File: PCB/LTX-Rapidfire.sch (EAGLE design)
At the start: 47 parts, among them J1 F-1X08-SIP-100-40Y, Q1 2N3904, Q10 SS8550D, Q11 2N3906, Q13 2N3904, Q2 2N3906, Q3 2N3904, Q4 2N3904, Q5 2N3904, Q6 2N3906, Q7 2N3906, Q8 2N3906, Q9 2N3904, SW1 F-1X02-SIP-100-40

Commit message: Whoops. Missed some bits. /Now/ it's complete.
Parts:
- added Q12: 2N3906, transistor-pnp:2N3906
- added R22: 100k, rcl:R-US_0204/2V
- added R23: 1k, rcl:R-US_0204/7
- added R26: 10k, rcl:R-US_0204/7
- R21: value 10k -> 200k
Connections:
- new net N$17: Q12.C, R23.1
- new net N$20: Q12.B, R21.2, R22.2
- net PA2: now also R26.2; no longer R21.2
- net PGND: now also R22.1
- net SGND: now also R23.2
- net SW9V: now also R21.1
- net VCC: now also Q12.E, R26.1; no longer R21.1
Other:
- moved on the sheet: R21
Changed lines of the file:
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@@
 <part name="U$1" library="izzy" deviceset="Z8F082A" device="DIL-8"/>
 <part name="SV1" library="izzy" deviceset="MA03-2" device=""/>
-<part name="R21" library="rcl" deviceset="R-US_" device="0204/7" value="10k"/>
+<part name="R26" library="rcl" deviceset="R-US_" device="0204/7" value="10k"/>
+<part name="R21" library="rcl" deviceset="R-US_" device="0204/7" value="200k"/>
+<part name="R22" library="rcl" deviceset="R-US_" device="0204/2V" value="100k"/>
+<part name="R23" library="rcl" deviceset="R-US_" device="0204/7" value="1k"/>
+<part name="Q12" library="transistor-pnp" deviceset="2N3906" device=""/>
 </parts>
 <sheets>
@@
 <instance part="U$1" gate="G$1" x="175.26" y="81.28"/>
 <instance part="SV1" gate="1" x="142.24" y="45.72"/>
-<instance part="R21" gate="G$1" x="142.24" y="35.56" rot="R180"/>
+<instance part="R26" gate="G$1" x="142.24" y="35.56" rot="R180"/>
+<instance part="R21" gate="G$1" x="88.9" y="50.8" rot="R270"/>
+<instance part="R22" gate="G$1" x="88.9" y="35.56" rot="R90"/>
+<instance part="R23" gate="G$1" x="106.68" y="30.48" rot="R270"/>
+<instance part="Q12" gate="G$1" x="104.14" y="43.18"/>
 </instances>
 <busses>
@@
 <label x="238.76" y="198.12" size="1.778" layer="95"/>
 </segment>
+<segment>
+<pinref part="R21" gate="G$1" pin="1"/>
+<wire x1="88.9" y1="55.88" x2="88.9" y2="58.42" width="0.1524" layer="91"/>
+<label x="88.9" y="58.42" size="1.778" layer="95" rot="R90"/>
+</segment>
 </net>
 <net name="LAZERMOD" class="0">
@@
 <label x="154.94" y="48.26" size="1.778" layer="95"/>
 </segment>
+<segment>
+<pinref part="R23" gate="G$1" pin="2"/>
+<wire x1="106.68" y1="25.4" x2="106.68" y2="22.86" width="0.1524" layer="91"/>
+<label x="106.68" y="22.86" size="1.778" layer="95" rot="R270"/>
+</segment>
 </net>
 <net name="PGND" class="0">
@@
 <wire x1="215.9" y1="177.8" x2="215.9" y2="175.26" width="0.1524" layer="91"/>
 <label x="215.9" y="175.26" size="1.778" layer="95" rot="R270"/>
+</segment>
+<segment>
+<pinref part="R22" gate="G$1" pin="1"/>
+<wire x1="88.9" y1="30.48" x2="88.9" y2="27.94" width="0.1524" layer="91"/>
+<label x="88.9" y="27.94" size="1.778" layer="95" rot="R270"/>
 </segment>
 </net>
@@
 <junction x="152.4" y="43.18"/>
 <label x="154.94" y="43.18" size="1.778" layer="95"/>
-<pinref part="R21" gate="G$1" pin="1"/>
+<pinref part="R26" gate="G$1" pin="1"/>
+</segment>
+<segment>
+<pinref part="Q12" gate="G$1" pin="E"/>
+<wire x1="106.68" y1="48.26" x2="106.68" y2="58.42" width="0.1524" layer="91"/>
+<label x="106.68" y="58.42" size="1.778" layer="95" rot="R90"/>
 </segment>
 </net>
@@
 <junction x="132.08" y="43.18"/>
 <label x="129.54" y="43.18" size="1.778" layer="95" rot="R180"/>
-<pinref part="R21" gate="G$1" pin="2"/>
+<pinref part="R26" gate="G$1" pin="2"/>
 </segment>
 </net>
@@
 </segment>
 </net>
+<net name="N$17" class="0">
+<segment>
+<pinref part="Q12" gate="G$1" pin="C"/>
+<pinref part="R23" gate="G$1" pin="1"/>
+<wire x1="106.68" y1="35.56" x2="106.68" y2="38.1" width="0.1524" layer="91"/>
+</segment>
+</net>
+<net name="N$20" class="0">
+<segment>
+<pinref part="R21" gate="G$1" pin="2"/>
+<pinref part="R22" gate="G$1" pin="2"/>
+<wire x1="88.9" y1="45.72" x2="88.9" y2="43.18" width="0.1524" layer="91"/>
+<pinref part="Q12" gate="G$1" pin="B"/>
+<wire x1="88.9" y1="43.18" x2="88.9" y2="40.64" width="0.1524" layer="91"/>
+<wire x1="101.6" y1="43.18" x2="88.9" y2="43.18" width="0.1524" layer="91"/>
+<junction x="88.9" y="43.18"/>
+</segment>
+</net>

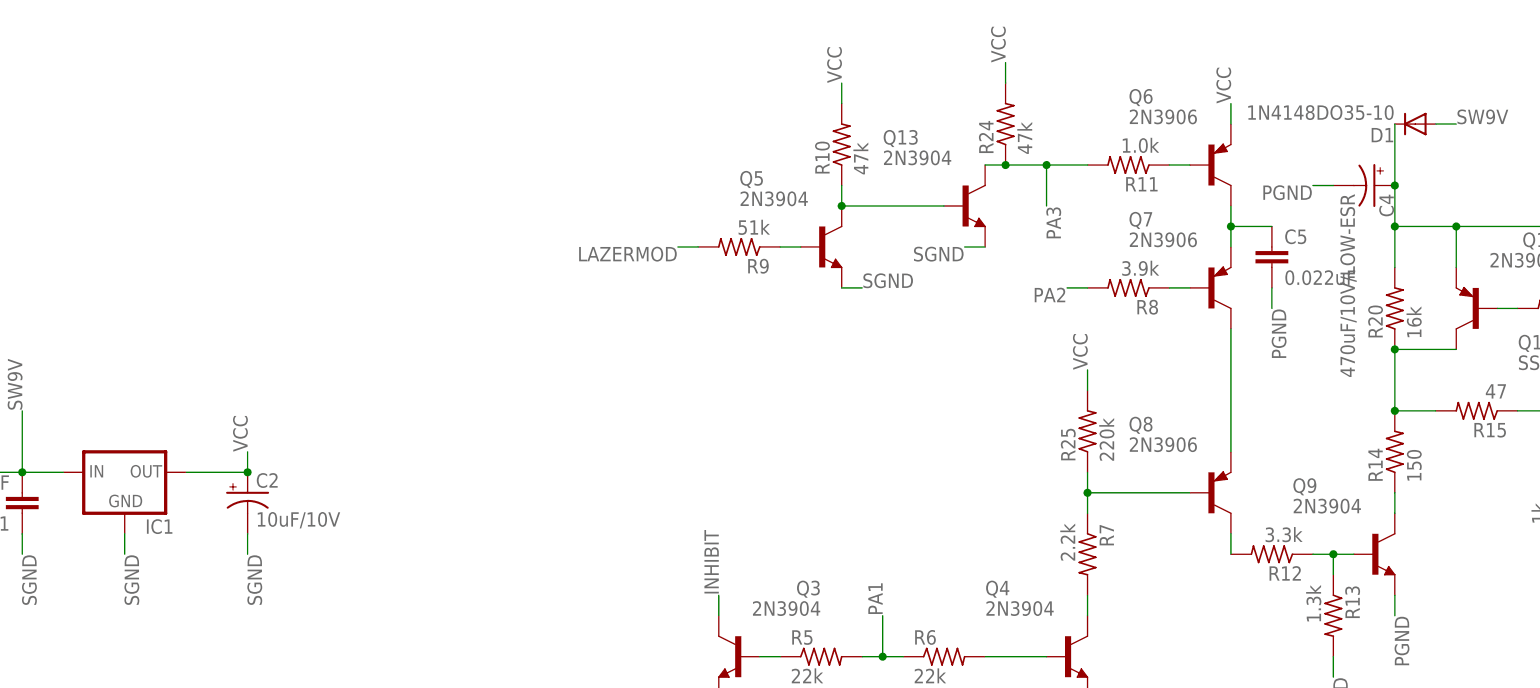
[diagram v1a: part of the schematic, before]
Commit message: First pass of PCB layout is complete.
Cleanup is in progress, but they should technically work as-is. Labels
are going to be impossible to see, though.
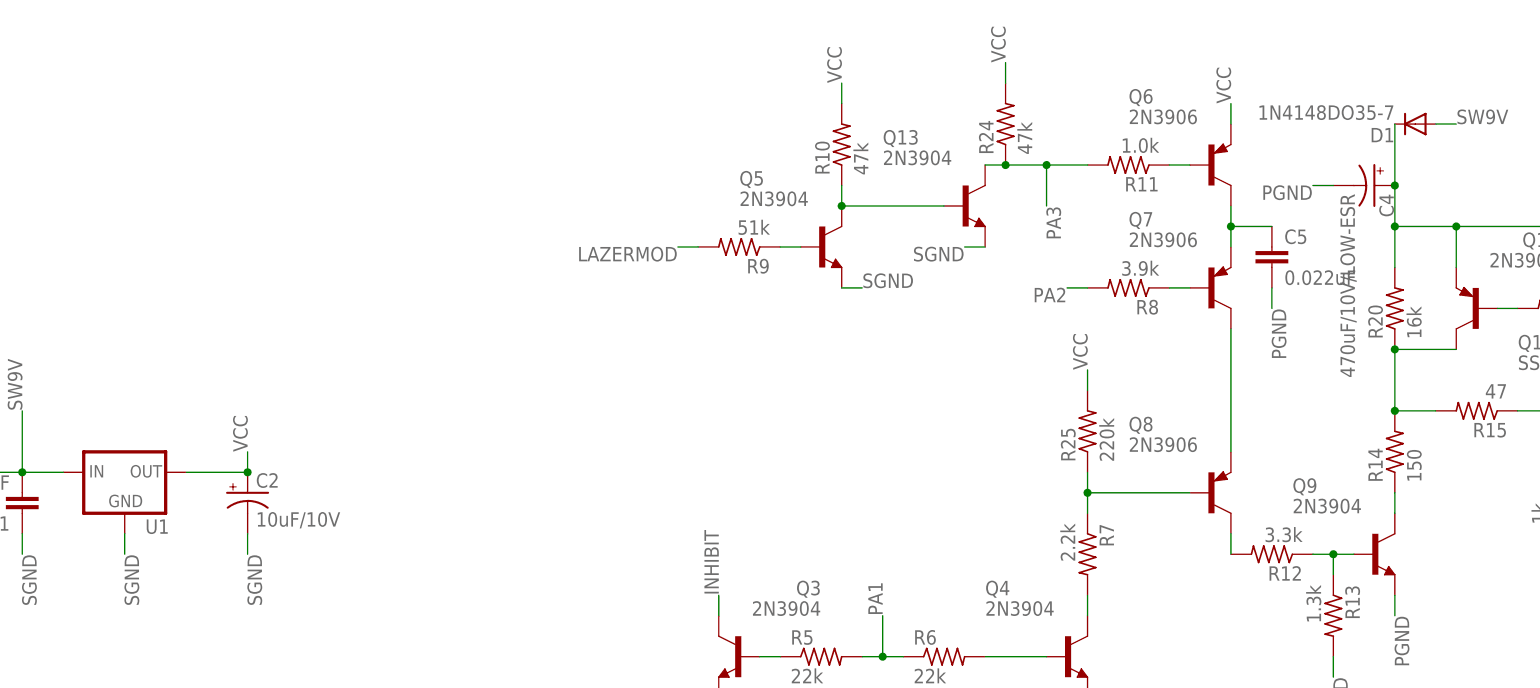
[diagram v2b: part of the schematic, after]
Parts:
- D1: value 1N4148DO35-10 -> 1N4148DO35-7; device diode:1N4148DO35-10 -> diode:1N4148DO35-7
- R26: device rcl:R-US_0204/7 -> rcl:R-US_0204/2V
- renumbered IC1 to U1
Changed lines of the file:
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@@
 <grid distance="0.1" unitdist="inch" unit="inch" style="lines" multiple="1" display="no" altdistance="0.01" altunitdist="inch" altunit="inch"/>
 <layers>
-<layer number="1" name="Top" color="4" fill="1" visible="no" active="no"/>
-<layer number="16" name="Bottom" color="1" fill="1" visible="no" active="no"/>
-<layer number="17" name="Pads" color="2" fill="1" visible="no" active="no"/>
-<layer number="18" name="Vias" color="2" fill="1" visible="no" active="no"/>
-<layer number="19" name="Unrouted" color="6" fill="1" visible="no" active="no"/>
-<layer number="20" name="Dimension" color="15" fill="1" visible="no" active="no"/>
-<layer number="21" name="tPlace" color="7" fill="1" visible="no" active="no"/>
-<layer number="22" name="bPlace" color="7" fill="1" visible="no" active="no"/>
-<layer number="23" name="tOrigins" color="15" fill="1" visible="no" active="no"/>
-<layer number="24" name="bOrigins" color="15" fill="1" visible="no" active="no"/>
-<layer number="25" name="tNames" color="7" fill="1" visible="no" active="no"/>
-<layer number="26" name="bNames" color="7" fill="1" visible="no" active="no"/>
-<layer number="27" name="tValues" color="7" fill="1" visible="no" active="no"/>
-<layer number="28" name="bValues" color="7" fill="1" visible="no" active="no"/>
+<layer number="1" name="Top" color="4" fill="1" visible="yes" active="no"/>
+<layer number="16" name="Bottom" color="1" fill="1" visible="yes" active="no"/>
+<layer number="17" name="Pads" color="2" fill="1" visible="yes" active="no"/>
+<layer number="18" name="Vias" color="2" fill="1" visible="yes" active="no"/>
+<layer number="19" name="Unrouted" color="6" fill="1" visible="yes" active="no"/>
+<layer number="20" name="Dimension" color="15" fill="1" visible="yes" active="no"/>
+<layer number="21" name="tPlace" color="7" fill="1" visible="yes" active="no"/>
+<layer number="22" name="bPlace" color="7" fill="1" visible="yes" active="no"/>
+<layer number="23" name="tOrigins" color="15" fill="1" visible="yes" active="no"/>
+<layer number="24" name="bOrigins" color="15" fill="1" visible="yes" active="no"/>
+<layer number="25" name="tNames" color="7" fill="1" visible="yes" active="no"/>
+<layer number="26" name="bNames" color="7" fill="1" visible="yes" active="no"/>
+<layer number="27" name="tValues" color="7" fill="1" visible="yes" active="no"/>
+<layer number="28" name="bValues" color="7" fill="1" visible="yes" active="no"/>
 <layer number="29" name="tStop" color="7" fill="3" visible="no" active="no"/>
 <layer number="30" name="bStop" color="7" fill="6" visible="no" active="no"/>
@@
 <layer number="35" name="tGlue" color="7" fill="4" visible="no" active="no"/>
 <layer number="36" name="bGlue" color="7" fill="5" visible="no" active="no"/>
-<layer number="37" name="tTest" color="7" fill="1" visible="no" active="no"/>
-<layer number="38" name="bTest" color="7" fill="1" visible="no" active="no"/>
+<layer number="37" name="tTest" color="7" fill="1" visible="yes" active="no"/>
+<layer number="38" name="bTest" color="7" fill="1" visible="yes" active="no"/>
 <layer number="39" name="tKeepout" color="4" fill="11" visible="no" active="no"/>
 <layer number="40" name="bKeepout" color="1" fill="11" visible="no" active="no"/>
@@
 <layer number="44" name="Drills" color="7" fill="1" visible="no" active="no"/>
 <layer number="45" name="Holes" color="7" fill="1" visible="no" active="no"/>
-<layer number="46" name="Milling" color="3" fill="1" visible="no" active="no"/>
-<layer number="47" name="Measures" color="7" fill="1" visible="no" active="no"/>
-<layer number="48" name="Document" color="7" fill="1" visible="no" active="no"/>
-<layer number="49" name="Reference" color="7" fill="1" visible="no" active="no"/>
-<layer number="50" name="dxf" color="7" fill="1" visible="no" active="no"/>
-<layer number="51" name="tDocu" color="7" fill="1" visible="no" active="no"/>
-<layer number="52" name="bDocu" color="7" fill="1" visible="no" active="no"/>
-<layer number="53" name="tGND_GNDA" color="7" fill="9" visible="no" active="no"/>
-<layer number="54" name="bGND_GNDA" color="1" fill="9" visible="no" active="no"/>
-<layer number="56" name="wert" color="7" fill="1" visible="no" active="no"/>
+<layer number="46" name="Milling" color="3" fill="1" visible="yes" active="no"/>
+<layer number="47" name="Measures" color="7" fill="1" visible="yes" active="no"/>
+<layer number="48" name="Document" color="7" fill="1" visible="yes" active="no"/>
+<layer number="49" name="Reference" color="7" fill="1" visible="yes" active="no"/>
+<layer number="50" name="dxf" color="7" fill="1" visible="yes" active="no"/>
+<layer number="51" name="tDocu" color="7" fill="1" visible="yes" active="no"/>
+<layer number="52" name="bDocu" color="7" fill="1" visible="yes" active="no"/>
+<layer number="53" name="tGND_GNDA" color="7" fill="9" visible="yes" active="no"/>
+<layer number="54" name="bGND_GNDA" color="1" fill="9" visible="yes" active="no"/>
+<layer number="56" name="wert" color="7" fill="1" visible="yes" active="no"/>
 <layer number="91" name="Nets" color="2" fill="1" visible="yes" active="yes"/>
 <layer number="92" name="Busses" color="1" fill="1" visible="yes" active="yes"/>
@@
 <part name="FRAME1" library="frames" deviceset="FRAME_A_L" device=""/>
 <part name="J1" library="con-headers-jp" deviceset="F-1X08-" device="SIP-100-40Y"/>
-<part name="IC1" library="v-reg" deviceset="78LXX" device=""/>
+<part name="U1" library="v-reg" deviceset="78LXX" device=""/>
 <part name="C1" library="rcl" deviceset="C-EU" device="025-025X050" value="0.1uF"/>
 <part name="C2" library="rcl" deviceset="CPOL-US" device="E2-4" value="10uF/10V"/>
-<part name="D1" library="diode" deviceset="1N4148" device="DO35-10"/>
+<part name="D1" library="diode" deviceset="1N4148" device="DO35-7" value="1N4148DO35-7"/>
 <part name="C4" library="rcl" deviceset="CPOL-US" device="E3.5-8" value="470uF/10V/LOW-ESR"/>
 <part name="R20" library="rcl" deviceset="R-US_" device="0204/2V" value="16k"/>
@@
 <part name="U$1" library="izzy" deviceset="Z8F082A" device="DIL-8"/>
 <part name="SV1" library="izzy" deviceset="MA03-2" device=""/>
-<part name="R26" library="rcl" deviceset="R-US_" device="0204/7" value="10k"/>
+<part name="R26" library="rcl" deviceset="R-US_" device="0204/2V" value="10k"/>
 <part name="R21" library="rcl" deviceset="R-US_" device="0204/7" value="200k"/>
 <part name="R22" library="rcl" deviceset="R-US_" device="0204/2V" value="100k"/>
@@
 <instance part="FRAME1" gate="G$2" x="172.72" y="0"/>
 <instance part="J1" gate="G$1" x="25.4" y="147.32" rot="MR0"/>
-<instance part="IC1" gate="1" x="73.66" y="154.94"/>
+<instance part="U1" gate="1" x="73.66" y="154.94"/>
 <instance part="C1" gate="G$1" x="60.96" y="149.86" rot="R180"/>
 <instance part="C2" gate="G$1" x="88.9" y="152.4"/>
@@
 <segment>
 <pinref part="C1" gate="G$1" pin="2"/>
-<pinref part="IC1" gate="1" pin="IN"/>
+<pinref part="U1" gate="1" pin="IN"/>
 <wire x1="60.96" y1="154.94" x2="66.04" y2="154.94" width="0.1524" layer="91"/>
 <pinref part="J1" gate="G$1" pin="1"/>
@@
 </segment>
 <segment>
-<pinref part="IC1" gate="1" pin="GND"/>
+<pinref part="U1" gate="1" pin="GND"/>
 <wire x1="73.66" y1="147.32" x2="73.66" y2="144.78" width="0.1524" layer="91"/>
 <label x="73.66" y="144.78" size="1.778" layer="95" rot="R270"/>
@@
 <net name="VCC" class="0">
 <segment>
-<pinref part="IC1" gate="1" pin="OUT"/>
+<pinref part="U1" gate="1" pin="OUT"/>
 <pinref part="C2" gate="G$1" pin="+"/>
 <wire x1="81.28" y1="154.94" x2="88.9" y2="154.94" width="0.1524" layer="91"/>
